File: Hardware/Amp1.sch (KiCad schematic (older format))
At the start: 23 parts

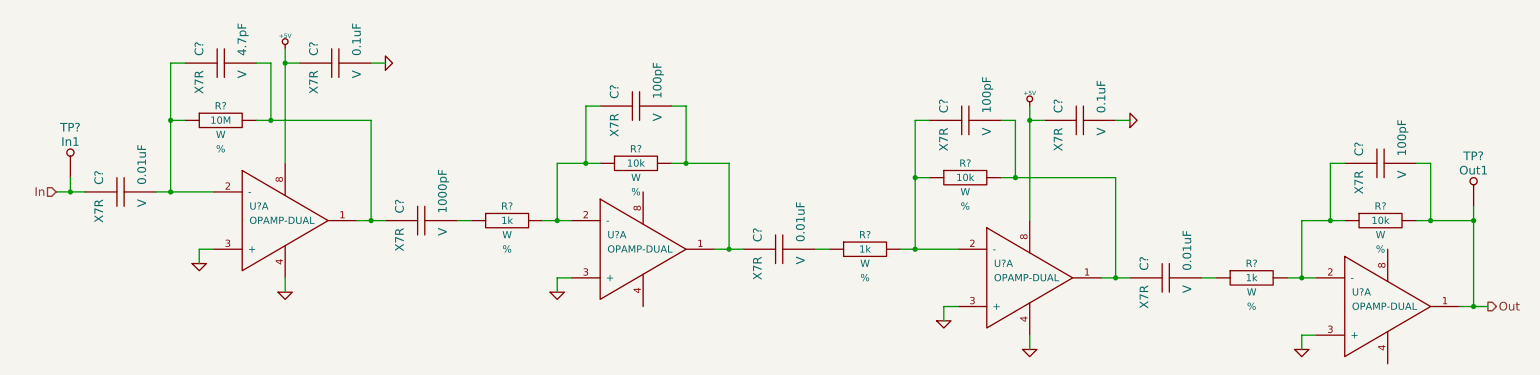
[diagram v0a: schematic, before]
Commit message: Add detector and coincidence sections
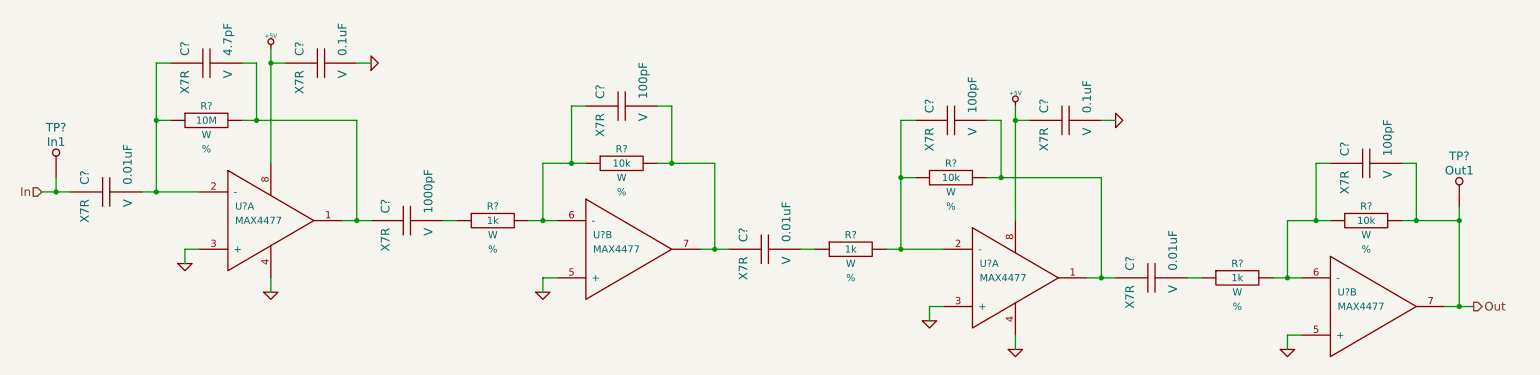
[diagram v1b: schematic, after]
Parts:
- removed U? (x2): OPAMP-DUAL, ~, symbol OPAMP-DUAL
- removed U?: OPAMP-DUAL, symbol OPAMP-DUAL
- added U? (x3): MAX4477, symbol OPAMP-DUAL
- U?: value OPAMP-DUAL -> MAX4477; Distributor Part No (none) -> MAX4477AUA+-ND; MFR Name (none) -> Maxim; MFR Part No (none) -> MAX4477AUA+
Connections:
- net +5V: now also U?.8
- net GND: now also U?.3 (+), U?.4, U?.5 (+), U?.5 (+)
- net Out: now also U?.7
- net at C?.1, C?.2, R?.2: now also U?.7
- net at C?.1, R?.1, R?.2: now also U?.6 (-) (x2)
- net at C?.1, R?.1, R?.2: now also U?.2 (-)
- net at C?.1, C?.2, R?.2: now also U?.1
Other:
- moved on the sheet: C?, R?, TP?, U?A

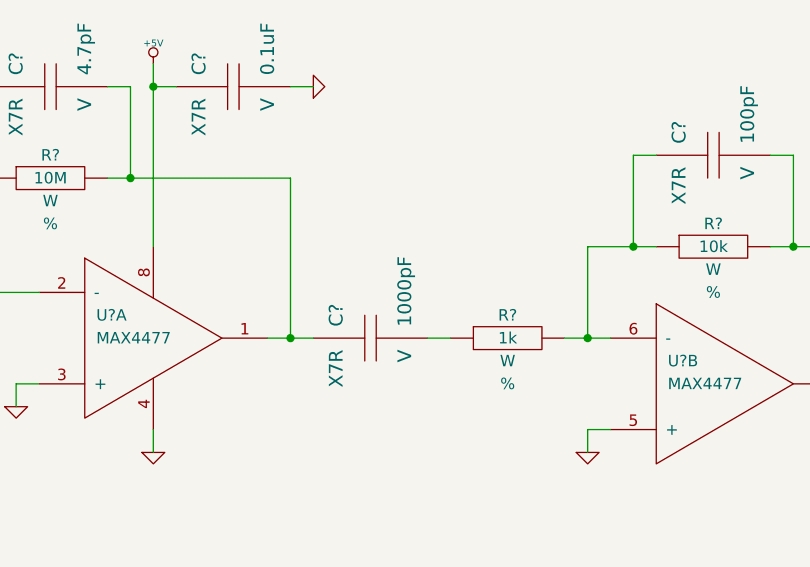
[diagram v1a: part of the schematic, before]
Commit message: Add processor support circuitry
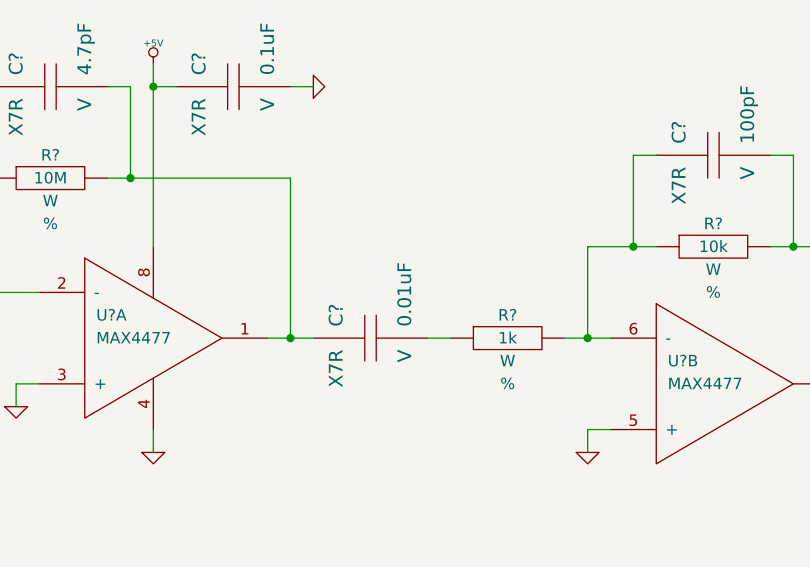
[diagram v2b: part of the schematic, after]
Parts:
- removed C?: 1000pF, ~, symbol C
- added C?: 0.01uF, ~, symbol C
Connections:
- net at C?.2, R?.2, U?.1: now also C?.1
- net at R?.1: now also C?.2
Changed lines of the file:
@@
 $Descr A4 11693 8268
 encoding utf-8
-Sheet 3 4
+Sheet 3 5
 Title "Solid State Cosmic Ray Detector"
-Date "23 sep 2013"
+Date "24 sep 2013"
 Rev "1"
 Comp "Ethan Harstad"
@@
 $EndComp
 $Comp
-L C C?
-U 1 1 523CFF05
-P 3350 3700
-F 0 "C?" H 3400 3850 60  0000 L CNN
-F 1 "1000pF" H 3400 3550 60  0000 L CNN
-F 2 "~" H 3350 3700 60  0000 C CNN
-F 3 "~" H 3350 3700 60  0000 C CNN
-F 4 "V" H 3300 3550 60  0000 R CNN "Voltage"
-F 5 "X7R" H 3300 3850 60  0000 R CNN "Dielectric"
-	1    3350 3700
-	0    -1   -1   0
-$EndComp
-$Comp
 L R R?
 U 1 1 523CFF0D
@@
 	1    0    0    -1
 $EndComp
+$Comp
+L C C?
+U 1 1 52410D12
+P 3350 3700
+F 0 "C?" H 3400 3850 60  0000 L CNN
+F 1 "0.01uF" H 3400 3550 60  0000 L CNN
+F 2 "~" H 3350 3700 60  0000 C CNN
+F 3 "~" H 3350 3700 60  0000 C CNN
+F 4 "V" H 3300 3550 60  0000 R CNN "Voltage"
+F 5 "X7R" H 3300 3850 60  0000 R CNN "Dielectric"
+	1    3350 3700
+	0    -1   -1   0
+$EndComp
 $EndSCHEMATC

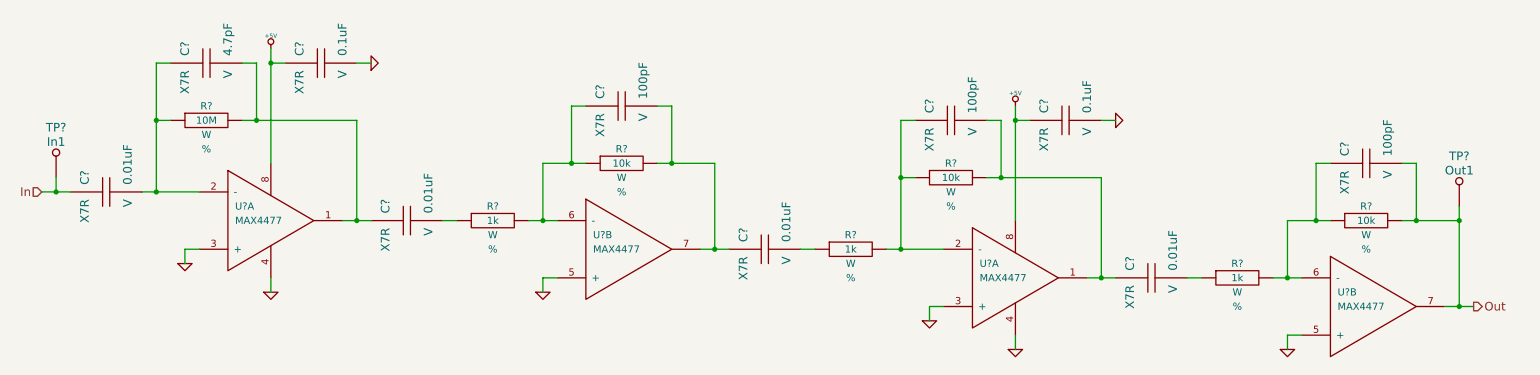
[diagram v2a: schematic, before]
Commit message: Fill BOM fields for detector section
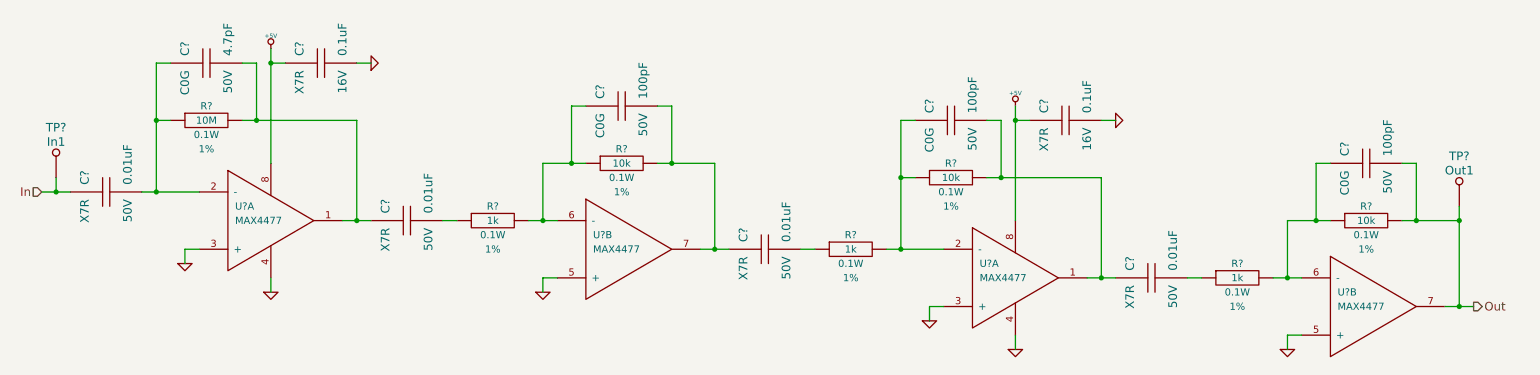
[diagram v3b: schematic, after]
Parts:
- removed C? (x3): 0.01uF, ~, symbol C
- removed C? (x2): 100pF, ~, symbol C
- removed C?: 0.1uF, ~, symbol C
- removed R? (x2): 1k, ~, symbol R
- removed R? (x2): 10k, ~, symbol R
- added C? (x3): 0.01uF, CAPC1608, symbol C
- added C? (x2): 100pF, CAPC1608, symbol C
- added C?: 0.1uF, CAPC1608, symbol C
- added R? (x2): 1k, RESC1608, symbol R
- added R? (x2): 10k, RESC1608, symbol R
- C?: footprint ~ -> CAPC1608; Dielectric X7R -> C0G; Distributor Part No (none) -> 1276-1282-1-ND; MFR Name (none) -> Samsung; MFR Part No (none) -> CL10C4R7CB8NNNC; Voltage V -> 50V
- C?: footprint ~ -> CAPC1608; Distributor Part No (none) -> 1276-1005-1-ND; MFR Name (none) -> Samsung; MFR Part No (none) -> CL10B104KO8NNNC; Voltage V -> 16V
- C?: footprint ~ -> CAPC1608; Dielectric X7R -> C0G; Distributor Part No (none) -> 1276-1008-1-ND; MFR Name (none) -> Samsung; MFR Part No (none) -> CL10C101JB8NNNC; Voltage V -> 50V
- C?: footprint ~ -> CAPC1608; Distributor Part No (none) -> 1276-1921-1-ND; MFR Name (none) -> Samsung; MFR Part No (none) -> CL10B103KB8NCNC; Voltage V -> 50V
- R?: footprint ~ -> RESC1608; Distributor Part No (none) -> 311-10.0MHRCT-ND; MFR Name (none) -> Yageo; MFR Part No (none) -> RC0603FR-0710ML; Power W -> 0.1W; Tolerance % -> 1%
- R?: footprint ~ -> RESC1608; Distributor Part No (none) -> 311-1.00KHRCT-ND; MFR Name (none) -> Yageo; MFR Part No (none) -> RC0603FR-071KL; Power W -> 0.1W; Tolerance % -> 1%
- R?: footprint ~ -> RESC1608; Distributor Part No (none) -> 311-10.0KHRCT-ND; MFR Name (none) -> Yageo; MFR Part No (none) -> RC0603FR-0710KL; Power W -> 0.1W; Tolerance % -> 1%
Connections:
- net +5V: now also C?.1
- net GND: now also C?.2
- net Out: now also C?.2, R?.2
- net at C?.2, R?.2, U?.1: now also C?.1
- net at R?.1: now also C?.2
- net at C?.2, R?.2, U?.7: now also C?.1
- net at U?.2 (-): now also C?.1, R?.1, R?.2
- net at U?.1: now also C?.1, C?.2, R?.2
- net at U?.6 (-): now also C?.1, R?.1, R?.2
- new net: C?.2, R?.1 (x2)
